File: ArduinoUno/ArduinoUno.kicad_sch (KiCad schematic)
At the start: 60 parts, among them J1 Jack_DC, J2 USB_B, J3 ICPSx, J4 Conn_02x02, J5 POWER, J6 ICPSx, J7 Header_10P, J8 ANALOG, J9 DIGITAL IO, Q1 FDN304V, SW1 SW_Push_NO, U1 MC33269-SOT, U2 ATmega16U2-M, U3 LM358D, U4 LP2985-3.3, U5 ATmega328-P, Y1 16MHz, Y2 16MHz

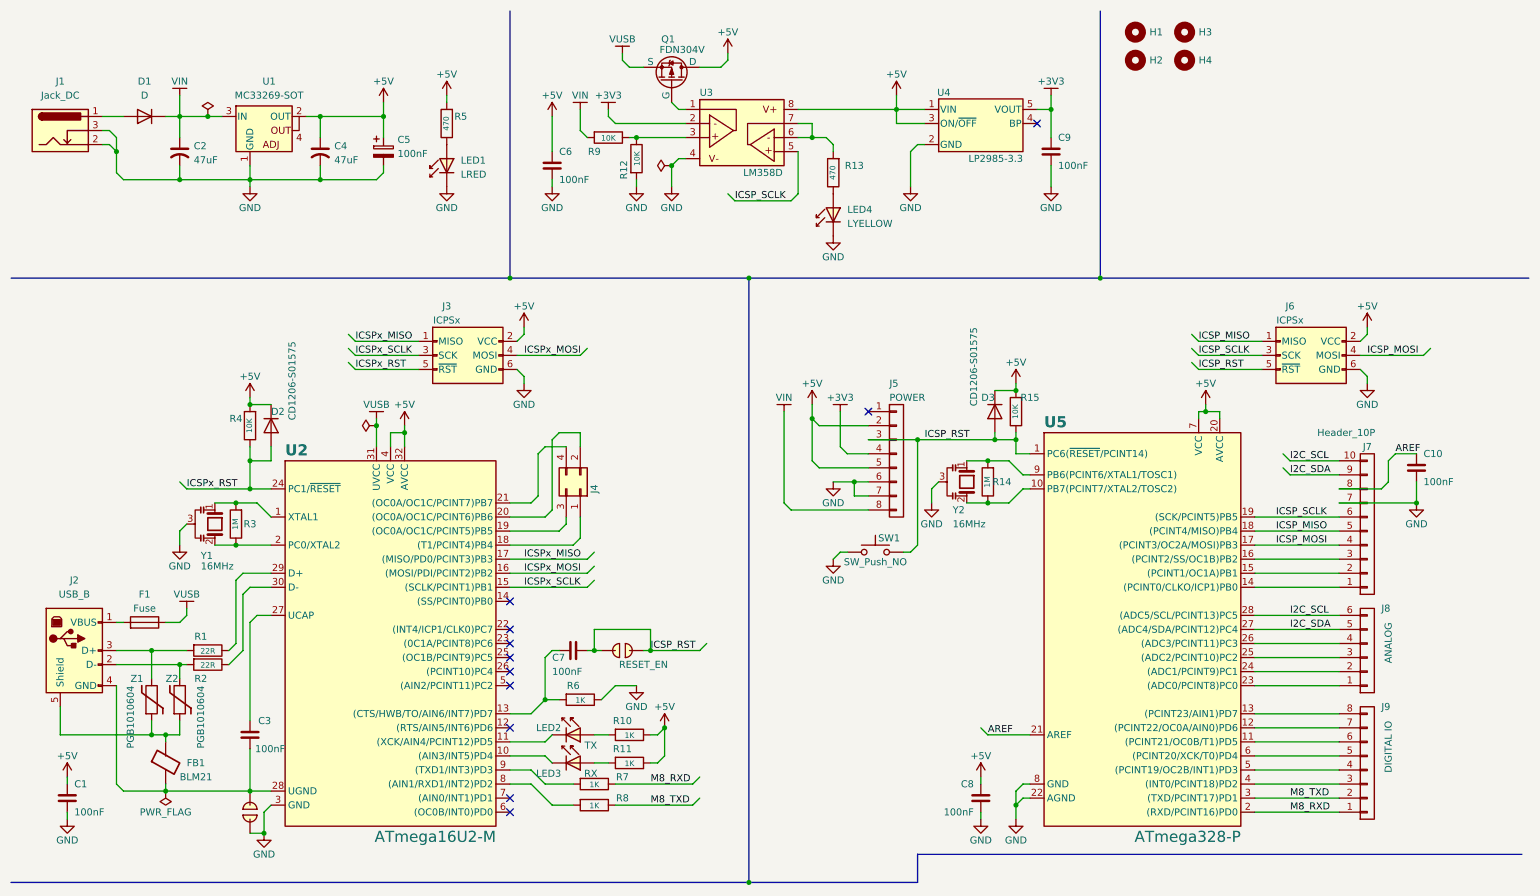
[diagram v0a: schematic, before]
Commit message: Arduino CH340
Change footprint, 3D model etc
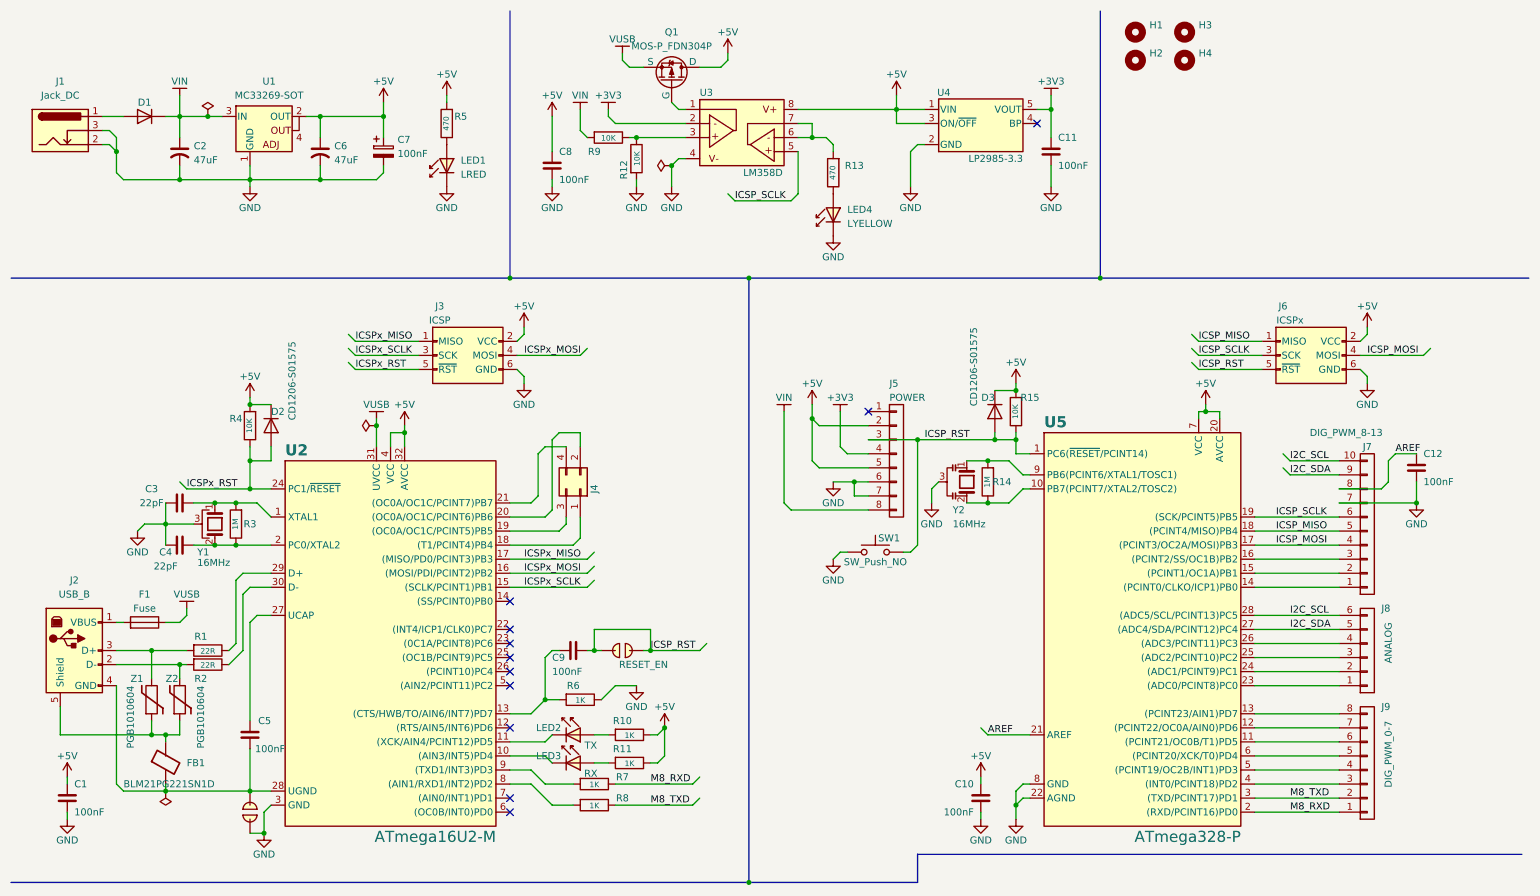
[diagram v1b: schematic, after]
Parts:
- removed C2, C4: 47uF, symbol 0pyzPassive:C_Polar
- removed D1: D, 0pyzActive:D_SMA, symbol 0pyzActive:D
- removed H1, H2, H3, H4: Hole, symbol 0pyzGeneral:MountingHole
- removed J1: Jack_DC, 0pyzConnector:JackDC_Input_3.5mm, symbol 0pyzConnector:Jack_DC
- removed J2: USB_B, 0pyzConnector:USB_B_Lumberg_2411_02_Horizontal, symbol 0pyzConnector:USB_B
- removed J3, J6: ICPSx, 0pyzConnector:IDC-Header_2x03_P2.54mm_Vertical, symbol 0pyzConnector:AVR-ISP-6
- removed LED1: LRED, 0pyzActive:LED_0805_2012Metric, symbol 0pyzActive:LRED
- removed LED2: TX, 0pyzActive:LED_0805_2012Metric, symbol 0pyzActive:LYELLOW
- removed LED3: RX, 0pyzActive:LED_0805_2012Metric, symbol 0pyzActive:LYELLOW
- removed LED4: LYELLOW, 0pyzActive:LED_0805_2012Metric, symbol 0pyzActive:LYELLOW
- removed Q1: FDN304V, symbol 0pyzActive:MOS-P_FDN304P
- removed U1: MC33269-SOT, 0pyzIC_MCU:SOT-223, symbol 0pyzIC_MCU:MC33269-SOT
- removed U2: ATmega16U2-M, Package_DFN_QFN:QFN-32-1EP_5x5mm_P0.5mm_EP3.1x3.1mm, symbol 0pyzIC_MCU:ATmega16U2-M
- removed U3: LM358D, 0pyzIC_MCU:SOIC-8-1EP_3.9x4.9mm_P1.27mm_EP2.29x3mm_ThermalVias, symbol 0pyzIC_MCU:LM358D
- removed U4: LP2985-3.3, Package_TO_SOT_SMD:SOT-23-5, symbol 0pyzIC_MCU:LP2985-3.3
- removed Y1: 16MHz, symbol 0pyzPassive:Crystal_C_GND
- added C2, C6: 47uF, 02pyzPassive:C_Radial_D4.0mm_H5.0mm_P1.50mm, symbol 02pyzPassive:C_Polar
- added C3, C4: 22pF, 02pyzPassive:C_0805_HandSolder, symbol 02pyzPassive:C
- added D1: D, 03pyzActive:D_SMA, symbol 03pyzActive:D
- added H1, H2, H3, H4: MountingHole, 01pyzGeneral:MountingHole_3.2mm_M3, symbol 01pyzGeneral:MountingHole
- added J1: Jack_DC, 04pyzConnector:JackDC_Input_3.5mm, symbol 04pyzConnector:Jack_DC
- added J2: USB_B, 04pyzConnector:USB_B_Lumberg_2411_02_Horizontal, symbol 04pyzConnector:USB_B
- added J3: ICSP, 04pyzConnector:PinHeader_2x03_P2.54mm_Vertical, symbol 04pyzConnector:AVR-ISP-6
- added J6: ICSPx, 04pyzConnector:PinHeader_2x03_P2.54mm_Vertical, symbol 04pyzConnector:AVR-ISP-6
- added LED1: LRED, 03pyzActive:D_0805_HandSolder, symbol 03pyzActive:LRED
- added LED2: TX, 03pyzActive:D_0805_HandSolder, symbol 03pyzActive:LYELLOW
- added LED3: RX, 03pyzActive:D_0805_HandSolder, symbol 03pyzActive:LYELLOW
- added LED4: LYELLOW, 03pyzActive:D_0805_HandSolder, symbol 03pyzActive:LYELLOW
- added Q1: MOS-P_FDN304P, 03pyzActive:SOT-23, symbol 03pyzActive:MOS-P_FDN304P
- added U1: MC33269-SOT, 07pyzIC_MCU:SOT-223, symbol 07pyzIC_MCU:MC33269-SOT
- added U2: ATmega16U2-M, Package_DFN_QFN:QFN-32-1EP_5x5mm_P0.5mm_EP3.1x3.1mm, symbol 07pyzIC_MCU:ATmega16U2-M
- added U3: LM358D, 07pyzIC_MCU:SOIC-8_3.9x4.9mm_P1.27mm, symbol 07pyzIC_MCU:LM358D
- added U4: LP2985-3.3, Package_TO_SOT_SMD:SOT-23-5, symbol 07pyzIC_MCU:LP2985-3.3
- added Y1: 16MHz, 02pyzPassive:Crystal_HC49-4H_Vertical_GND, symbol 02pyzPassive:Crystal_GND
- C1: footprint (none) -> 02pyzPassive:C_0805_HandSolder; symbol 0pyzPassive:C -> 02pyzPassive:C
- C10: renamed from C8; footprint (none) -> 02pyzPassive:C_0805_HandSolder; symbol 0pyzPassive:C -> 02pyzPassive:C
- C11: renamed from C9; footprint (none) -> 02pyzPassive:C_0805_HandSolder; symbol 0pyzPassive:C -> 02pyzPassive:C
- C12: renamed from C10; footprint (none) -> 02pyzPassive:C_0805_HandSolder; symbol 0pyzPassive:C -> 02pyzPassive:C
- C5: renamed from C3; footprint (none) -> 02pyzPassive:C_0805_HandSolder; symbol 0pyzPassive:C -> 02pyzPassive:C
- C7: renamed from C5; footprint 0pyzAllBasic:CP_EIA-3216-10_Kemet-I -> 02pyzPassive:CP_EIA-3216-10_Kemet-I; symbol 0pyzPassive:C_Tant -> 02pyzPassive:C_Tant
- C8: renamed from C6; footprint (none) -> 02pyzPassive:C_0805_HandSolder; symbol 0pyzPassive:C -> 02pyzPassive:C
- C9: renamed from C7; footprint (none) -> 02pyzPassive:C_0805_HandSolder; symbol 0pyzPassive:C -> 02pyzPassive:C
- D2, D3: footprint 0pyzActive:D_SMA -> 03pyzActive:D_1206_HandSolder; symbol 0pyzActive:D -> 03pyzActive:D
- F1: footprint (none) -> 02pyzPassive:C_1206_HandSolder; symbol 0pyzPassive:Fuse -> 02pyzPassive:Fuse
- FB1: value BLM21 -> BLM21PG221SN1D; footprint (none) -> 02pyzPassive:R_0603_HandSolder; symbol 0pyzPassive:FerriteBead -> 02pyzPassive:FerriteBead
- J4: footprint 0pyzConnector:PinHeader_2x02_P2.54mm_Vertical -> 04pyzConnector:PinHeader_2x02_P2.54mm_Vertical; symbol 0pyzConnector:Conn_02x02 -> 04pyzConnector:Conn_02x02
- J5: footprint 0pyzConnector:JST_XH_B8B-XH-A_1x08_P2.50mm_Vertical -> 04pyzConnector:PinSocket_1x08_P2.54mm_Vertical; symbol 0pyzConnector:Header_8P -> 04pyzConnector:Header_8P
- J7: value Header_10P -> DIG_PWM_8-13; footprint 0pyzConnector:JST_XH_B10B-XH-A_1x10_P2.50mm_Vertical -> 04pyzConnector:PinSocket_1x10_P2.54mm_Vertical; symbol 0pyzConnector:Header_10P -> 04pyzConnector:Header_10P
- J8: footprint 0pyzConnector:JST_XH_B6B-XH-A_1x06_P2.50mm_Vertical -> 04pyzConnector:PinSocket_1x06_P2.54mm_Vertical; symbol 0pyzConnector:Header_6P -> 04pyzConnector:Header_6P
- J9: value DIGITAL IO -> DIG_PWM_0-7; footprint 0pyzConnector:JST_XH_B8B-XH-A_1x08_P2.50mm_Vertical -> 04pyzConnector:PinSocket_1x08_P2.54mm_Vertical; symbol 0pyzConnector:Header_8P -> 04pyzConnector:Header_8P
- R1, R10, R11, R12, R13, R14, R15, R2, R3, R4, R5, R6, R7, R8, R9: footprint 0pyzPassive:R_0805_2012Metric -> 02pyzPassive:R_0805_HandSolder; symbol 0pyzPassive:R -> 02pyzPassive:R
- SOL1, SOL2: footprint (none) -> 01pyzGeneral:SolderJumper-2_P1.3mm_Open_RoundedPad1.0x1.5mm; symbol 0pyzGeneral:SolderJumper -> 01pyzGeneral:SolderJumper
- SW1: footprint (none) -> 06pyzSwitchRelay:SW_SPST_CK_RS282G05A3; symbol 0pyzSwitchRelay:SW_Push_NO -> 06pyzSwitchRelay:SW_Push_NO
- U5: symbol 0pyzIC_MCU:ATmega328-P -> 07pyzIC_MCU:ATmega328-P
- Y2: footprint (none) -> 02pyzPassive:Resonator_SMD_Murata_CSTxExxV-3Pin_3.0x1.1mm_HandSoldering; symbol 0pyzPassive:Crystal_C_GND -> 02pyzPassive:Crystal_C_GND
- Z1, Z2: footprint (none) -> 02pyzPassive:C_0603_HandSolder; symbol 0pyzPassive:Varistor -> 02pyzPassive:Varistor
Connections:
- net +3V3: now also U3.2 (INPA-), U4.5 (VOUT)
- net +5V: now also C6.1, J3.2 (VCC), J6.2 (VCC), Q1.1 (D), U1.2 (OUT), U1.4 (OUT), U2.32 (AVCC), U2.4 (VCC), U3.8 (V+), U4.1 (VIN), U4.3 (ON/~{OFF})
- net GND: now also C2.2, C3.1, C4.1, C6.2, J1.2, J1.3, J3.6 (GND), J6.6 (GND), LED1.1 (K), LED4.1 (K), U1.1 (GND), U2.3 (GND), U2.33 (GND), U3.4 (V-), U4.2 (GND), Y1.3
- net ICSP_MISO: now also J6.1 (MISO)
- net ICSP_MOSI: now also J6.4 (MOSI)
- net ICSP_RST: now also J6.5 (~{RST})
- net ICSP_SCLK: now also J6.3 (SCK), U3.5 (INPB-)
- net ICSPx_MISO: now also J3.1 (MISO), U2.17 ((MISO/PD0/PCINT3)PB3)
- net ICSPx_MOSI: now also J3.4 (MOSI), U2.16 ((MOSI/PDI/PCINT2)PB2)
- net ICSPx_RST: now also J3.5 (~{RST}), U2.24 (PC1/~{RESET})
- net ICSPx_SCLK: now also J3.3 (SCK), U2.15 ((SCLK/PCINT1)PB1)
- net VIN: now also C2.1, D1.1 (K), U1.3 (IN)
- net VUSB: now also Q1.3 (S), U2.31 (UVCC)
- net at R11.1: now also LED3.2 (A)
- net at R3.1: now also C3.2, U2.1 (XTAL1), Y1.1
- net at R3.2: now also C4.2, U2.2 (PC0/XTAL2), Y1.2
- net at R10.1: now also LED2.2 (A)
- net at R12.2, R9.2: now also U3.3 (INPA+)
- net at J4.1 (Pin_1): now also U2.18 ((T1/PCINT4)PB4)
- net at J4.2 (Pin_2): now also U2.20 ((OC0A/OC1C/PCINT6)PB6)
- net at J4.3 (Pin_3): now also U2.19 ((OC0A/OC1C/PCINT5)PB5)
- net at J4.4 (Pin_4): now also U2.21 ((OC0A/OC1C/PCINT7)PB7)
- net at C9.2, R6.1: now also U2.13 ((CTS/HWB/TO/AIN6/INT7)PD7)
- net at F1.1: now also J2.1 (VBUS)
- net at R2.1, Z2.1: now also J2.2 (D-)
- net at R1.1, Z1.1: now also J2.3 (D+)
- net at C5.2, FB1.2, SOL1.2: now also J2.4 (GND), U2.28 (UGND)
- net at FB1.1, Z1.2, Z2.2: now also J2.5 (Shield)
- net at R5.2: now also LED1.2 (A)
- net at R8.1: now also U2.8 ((AIN1/RXD1/INT2)PD2)
- net at R1.2: now also U2.29 (D+)
- net at R13.1: now also U3.6 (INPB+), U3.7 (OUTB)
- net at R2.2: now also U2.30 (D-)
- net at C5.1: now also U2.27 (UCAP)
- net at R13.2: now also LED4.2 (A)
- net at R7.1: now also U2.9 ((TXD1/INT3)PD3)
- new net: D1.2 (A), J1.1
- new net: LED3.1 (K), U2.10 ((AIN3/INT5)PD4)
- new net: LED2.1 (K), U2.11 ((XCK/AIN4/PCINT12)PD5)
- new net: Q1.2 (G), U3.1 (OUTA)
